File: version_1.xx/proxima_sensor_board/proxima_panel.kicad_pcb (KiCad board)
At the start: 2 copper layers, 83 x 94 mm, 587 parts, among them J1 Conn_01x03, U1 TSOP32156, U2 NE555D

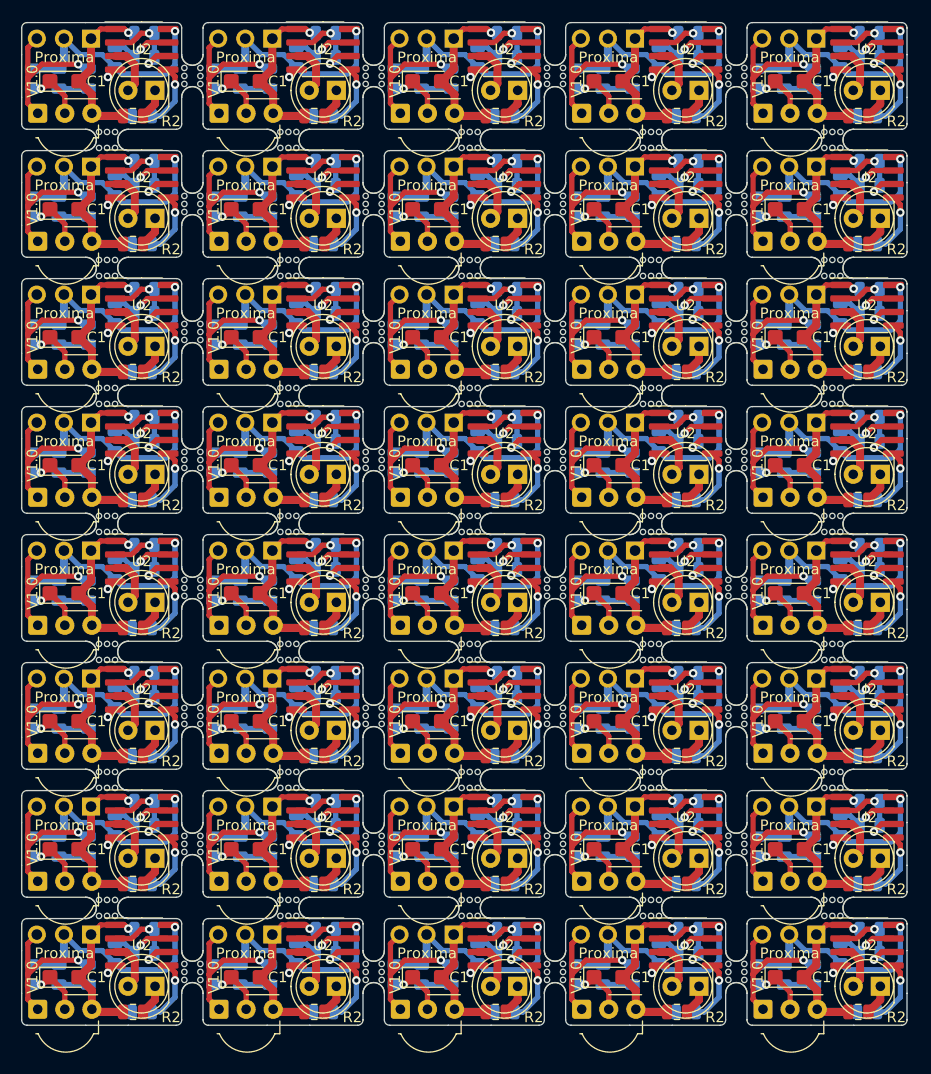
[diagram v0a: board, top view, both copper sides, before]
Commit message: 5mm breakway
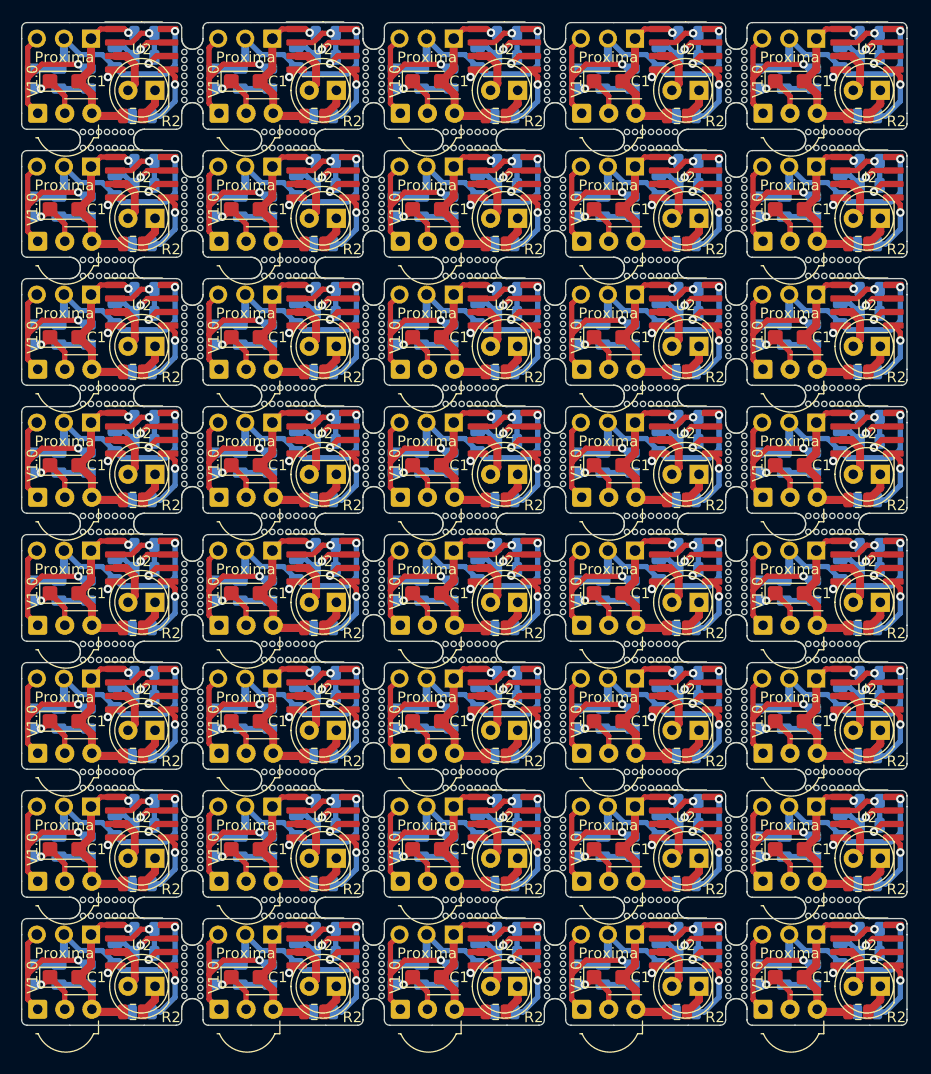
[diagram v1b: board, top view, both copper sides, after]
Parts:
- removed the C3 at (211.5, 134.0)
- removed the C3 at (211.5, 170.0)
- removed the R2 at (176.4, 105.8)
- removed the U1 at (167.5, 117.5)
- removed mouse-bite-2mm-slot (x64): VAL**, Panelization:mouse-bite-2mm-slot
- added ?: , , F.Cu at (165.0, 102.0)
- added ?: , , F.Cu at (199.0, 162.0)
- added ?: , , F.Cu at (182.0, 162.0)
- added ?: , , F.Cu at (165.0, 162.0)
- added ?: , , F.Cu at (148.0, 162.0)
- added ?: , , F.Cu at (199.0, 150.0)
- added ?: , , F.Cu at (182.0, 150.0)
- added ?: , , F.Cu at (165.0, 150.0)
- added ?: , , F.Cu at (148.0, 150.0)
- added ?: , , F.Cu at (199.0, 138.0)
- added ?: , , F.Cu at (182.0, 138.0)
- added ?: , , F.Cu at (199.0, 186.0)
- added ?: , , F.Cu at (165.0, 138.0)
- added ?: , , F.Cu at (148.0, 138.0)
- added ?: , , F.Cu at (199.0, 126.0)
- added ?: , , F.Cu at (182.0, 126.0)
- added ?: , , F.Cu at (165.0, 126.0)
- added ?: , , F.Cu at (148.0, 126.0)
- added ?: , , F.Cu at (199.0, 114.0)
- added ?: , , F.Cu at (182.0, 114.0)
- added ?: , , F.Cu at (165.0, 114.0)
- added ?: , , F.Cu at (148.0, 114.0)
- added ?: , , F.Cu at (182.0, 186.0)
- added ?: , , F.Cu at (199.0, 102.0)
- added ?: , , F.Cu at (182.0, 102.0)
- added ?: , , F.Cu at (208.0, 180.0)
- added ?: , , F.Cu at (191.0, 180.0)
- added ?: , , F.Cu at (174.0, 180.0)
- added ?: , , F.Cu at (157.0, 180.0)
- added ?: , , F.Cu at (140.0, 180.0)
- added ?: , , F.Cu at (208.0, 168.0)
- added ?: , , F.Cu at (191.0, 168.0)
- added ?: , , F.Cu at (174.0, 168.0)
- added ?: , , F.Cu at (165.0, 186.0)
- added ?: , , F.Cu at (157.0, 168.0)
- added ?: , , F.Cu at (140.0, 168.0)
- added ?: , , F.Cu at (208.0, 156.0)
- added ?: , , F.Cu at (191.0, 156.0)
- added ?: , , F.Cu at (174.0, 156.0)
- added ?: , , F.Cu at (157.0, 156.0)
- added ?: , , F.Cu at (140.0, 156.0)
- added ?: , , F.Cu at (208.0, 144.0)
- added ?: , , F.Cu at (191.0, 144.0)
- added ?: , , F.Cu at (174.0, 144.0)
- added ?: , , F.Cu at (148.0, 186.0)
- added ?: , , F.Cu at (157.0, 144.0)
- added ?: , , F.Cu at (140.0, 144.0)
- added ?: , , F.Cu at (208.0, 132.0)
- added ?: , , F.Cu at (191.0, 132.0)
- added ?: , , F.Cu at (174.0, 132.0)
- added ?: , , F.Cu at (157.0, 132.0)
- added ?: , , F.Cu at (140.0, 132.0)
- added ?: , , F.Cu at (208.0, 120.0)
- added ?: , , F.Cu at (191.0, 120.0)
- added ?: , , F.Cu at (174.0, 120.0)
- added ?: , , F.Cu at (199.0, 174.0)
- added ?: , , F.Cu at (157.0, 120.0)
- added ?: , , F.Cu at (140.0, 120.0)
- added ?: , , F.Cu at (208.0, 108.0)
- added ?: , , F.Cu at (191.0, 108.0)
- added ?: , , F.Cu at (174.0, 108.0)
- added ?: , , F.Cu at (157.0, 108.0)
- added ?: , , F.Cu at (140.0, 108.0)
- added ?: , , F.Cu at (148.0, 102.0)
- added ?: , , F.Cu at (182.0, 174.0)
- added ?: , , F.Cu at (165.0, 174.0)
- added ?: , , F.Cu at (148.0, 174.0)
- added R5: 500, Resistor_SMD:R_0805_2012Metric, B.Cu at (138.2, 186.2)
- C3 (x2): renamed from mouse-bite-2mm-slot; value VAL** -> 1.2nF; footprint Panelization:mouse-bite-2mm-slot -> Capacitor_SMD:C_0805_2012Metric; moved to B.Cu
- R2: renamed from mouse-bite-2mm-slot; value VAL** -> 47; footprint Panelization:mouse-bite-2mm-slot -> Resistor_SMD:R_0805_2012Metric
- U1: renamed from R5; value 500 -> TSOP32156; footprint Resistor_SMD:R_0805_2012Metric -> OptoDevice:Vishay_MOLD-3Pin; moved to F.Cu
- moved U1 74.7 mm to (167.5, 117.5), turned to 0 degrees
- moved R2 62.3 mm to (176.4, 105.8), turned to 180 degrees
- moved C3 33.1 mm to (211.5, 134.0), turned to 180 degrees
- moved C3 26.2 mm to (211.5, 170.0), turned to 180 degrees
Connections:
- U1 pad 1: Net-(D2-Pad1) -> OUTPUT_INVERTED
- U1 pad 2: OUTPUT_INVERTED -> Net-(C1-Pad1)
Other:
- outline, holes or cut-outs redrawn

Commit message: panelization 2
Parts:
- removed the ? at (199.0, 162.0)
- removed the ? at (182.0, 162.0)
- removed the ? at (165.0, 162.0)
- removed the ? at (148.0, 162.0)
- removed the ? at (199.0, 150.0)
- removed the ? at (182.0, 150.0)
- removed the ? at (165.0, 150.0)
- removed the ? at (148.0, 150.0)
- removed the ? at (199.0, 138.0)
- removed the ? at (182.0, 138.0)
- removed the ? at (199.0, 186.0)
- removed the ? at (165.0, 138.0)
- removed the ? at (148.0, 138.0)
- removed the ? at (199.0, 126.0)
- removed the ? at (182.0, 126.0)
- removed the ? at (165.0, 126.0)
- removed the ? at (148.0, 126.0)
- removed the ? at (199.0, 114.0)
- removed the ? at (182.0, 186.0)
- removed the ? at (199.0, 102.0)
- removed the ? at (182.0, 102.0)
- removed the ? at (208.0, 180.0)
- removed the ? at (191.0, 180.0)
- removed the ? at (174.0, 180.0)
- removed the ? at (157.0, 180.0)
- removed the ? at (140.0, 180.0)
- removed the ? at (208.0, 168.0)
- removed the ? at (191.0, 168.0)
- removed the ? at (174.0, 168.0)
- removed the ? at (165.0, 186.0)
- removed the ? at (157.0, 168.0)
- removed the ? at (140.0, 168.0)
- removed the ? at (208.0, 156.0)
- removed the ? at (191.0, 156.0)
- removed the ? at (174.0, 156.0)
- removed the ? at (157.0, 156.0)
- removed the ? at (140.0, 156.0)
- removed the ? at (208.0, 144.0)
- removed the ? at (191.0, 144.0)
- removed the ? at (174.0, 144.0)
- removed the ? at (148.0, 186.0)
- removed the ? at (157.0, 144.0)
- removed the ? at (140.0, 144.0)
- removed the ? at (208.0, 132.0)
- removed the ? at (191.0, 132.0)
- removed the ? at (174.0, 132.0)
- removed the ? at (157.0, 132.0)
- removed the ? at (140.0, 132.0)
- removed the ? at (208.0, 120.0)
- removed the ? at (191.0, 120.0)
- removed the ? at (174.0, 120.0)
- removed the ? at (199.0, 174.0)
- removed the ? at (157.0, 120.0)
- removed the ? at (140.0, 120.0)
- removed the ? at (208.0, 108.0)
- removed the ? at (191.0, 108.0)
- removed the ? at (182.0, 174.0)
- removed the ? at (165.0, 174.0)
- removed the ? at (148.0, 174.0)
- removed the C1 at (204.0, 186.5)
- removed the C1 at (136.0, 174.5)
- removed the C1 at (204.0, 162.5)
- removed the C1 at (187.0, 162.5)
- removed the C1 at (170.0, 162.5)
- removed the C1 at (153.0, 162.5)
- removed the C1 at (136.0, 162.5)
- removed the C1 at (204.0, 150.5)
- removed the C1 at (187.0, 150.5)
- removed the C1 at (170.0, 150.5)
- removed the C1 at (153.0, 150.5)
- removed the C1 at (187.0, 186.5)
- removed the C1 at (136.0, 150.5)
- removed the C1 at (204.0, 138.5)
- removed the C1 at (187.0, 138.5)
- removed the C1 at (170.0, 138.5)
- removed the C1 at (153.0, 138.5)
- removed the C1 at (136.0, 138.5)
- removed the C1 at (204.0, 126.5)
- removed the C1 at (187.0, 126.5)
- removed the C1 at (170.0, 126.5)
- removed the C1 at (153.0, 126.5)
- removed the C1 at (170.0, 186.5)
- removed the C1 at (136.0, 126.5)
- removed the C1 at (204.0, 114.5)
- removed the C1 at (187.0, 114.5)
- removed the C1 at (204.0, 102.5)
- removed the C1 at (187.0, 102.5)
- removed the C1 at (153.0, 186.5)
- removed the C1 at (136.0, 186.5)
- removed the C1 at (204.0, 174.5)
- removed the C1 at (187.0, 174.5)
- removed the C1 at (170.0, 174.5)
- removed the C1 at (153.0, 174.5)
- removed the C2 at (211.2, 189.8)
- removed the C2 at (143.2, 177.8)
- removed the C2 at (211.2, 165.8)
- removed the C2 at (194.2, 165.8)
- removed the C2 at (177.2, 165.8)
- removed the C2 at (160.2, 165.8)
- removed the C2 at (143.2, 165.8)
- removed the C2 at (211.2, 153.8)
- removed the C2 at (194.2, 153.8)
- removed the C2 at (177.2, 153.8)
- removed the C2 at (160.2, 153.8)
- removed the C2 at (194.2, 189.8)
- removed the C2 at (143.2, 153.8)
- removed the C2 at (211.2, 141.8)
- removed the C2 at (194.2, 141.8)
- removed the C2 at (177.2, 141.8)
- removed the C2 at (160.2, 141.8)
- removed the C2 at (143.2, 141.8)
- removed the C2 at (211.2, 129.8)
- removed the C2 at (194.2, 129.8)
- removed the C2 at (177.2, 129.8)
- removed the C2 at (160.2, 129.8)
- removed the C2 at (177.2, 189.8)
- removed the C2 at (143.2, 129.8)
- removed the C2 at (211.2, 117.8)
- removed the C2 at (194.2, 117.8)
- removed the C2 at (211.2, 105.8)
- removed the C2 at (194.2, 105.8)
- removed the C2 at (160.2, 189.8)
- removed the C2 at (143.2, 189.8)
- removed the C2 at (211.2, 177.8)
- removed the C2 at (194.2, 177.8)
- removed the C2 at (177.2, 177.8)
- removed the C2 at (160.2, 177.8)
- removed the C3 at (211.5, 182.0)
- removed the C3 at (143.5, 170.0)
- removed the C3 at (211.5, 158.0)
- removed the C3 at (194.5, 158.0)
- removed the C3 at (177.5, 158.0)
- removed the C3 at (160.5, 158.0)
- removed the C3 at (143.5, 158.0)
- removed the C3 at (211.5, 146.0)
- removed the C3 at (194.5, 146.0)
- removed the C3 at (177.5, 146.0)
- removed the C3 at (160.5, 146.0)
- removed the C3 at (194.5, 182.0)
- removed the C3 at (143.5, 146.0)
- removed the C3 at (211.5, 134.0)
- removed the C3 at (194.5, 134.0)
- removed the C3 at (177.5, 134.0)
- removed the C3 at (160.5, 134.0)
- removed the C3 at (143.5, 134.0)
- removed the C3 at (211.5, 122.0)
- removed the C3 at (194.5, 122.0)
- removed the C3 at (177.5, 122.0)
- removed the C3 at (160.5, 122.0)
- removed the C3 at (177.5, 182.0)
- removed the C3 at (143.5, 122.0)
- removed the C3 at (211.5, 110.0)
- removed the C3 at (194.5, 110.0)
- removed the C3 at (211.5, 98.0)
- removed the C3 at (194.5, 98.0)
- removed the C3 at (160.5, 182.0)
- removed the C3 at (143.5, 182.0)
- removed the C3 at (211.5, 170.0)
- removed the C3 at (194.5, 170.0)
- removed the C3 at (177.5, 170.0)
- removed the C3 at (160.5, 170.0)
- removed the D1 at (212.5, 187.3)
- removed the D1 at (144.5, 175.3)
- removed the D1 at (212.5, 163.3)
- removed the D1 at (195.5, 163.3)
- removed the D1 at (178.5, 163.3)
- removed the D1 at (161.5, 163.3)
- removed the D1 at (144.5, 163.3)
- removed the D1 at (212.5, 151.3)
- removed the D1 at (195.5, 151.3)
- removed the D1 at (178.5, 151.3)
- removed the D1 at (161.5, 151.3)
- removed the D1 at (195.5, 187.3)
- removed the D1 at (144.5, 151.3)
- removed the D1 at (212.5, 139.3)
- removed the D1 at (195.5, 139.3)
- removed the D1 at (178.5, 139.3)
- removed the D1 at (161.5, 139.3)
- removed the D1 at (144.5, 139.3)
- removed the D1 at (212.5, 127.3)
- removed the D1 at (195.5, 127.3)
- removed the D1 at (178.5, 127.3)
- removed the D1 at (161.5, 127.3)
- removed the D1 at (178.5, 187.3)
- removed the D1 at (144.5, 127.3)
- removed the D1 at (212.5, 115.3)
- removed the D1 at (195.5, 115.3)
- removed the D1 at (212.5, 103.3)
- removed the D1 at (195.5, 103.3)
- removed the D1 at (161.5, 187.3)
- removed the D1 at (144.5, 187.3)
- removed the D1 at (212.5, 175.3)
- removed the D1 at (195.5, 175.3)
- removed the D1 at (178.5, 175.3)
- removed the D1 at (161.5, 175.3)
- removed the D2 at (203.5, 186.2)
- removed the D2 at (135.5, 174.2)
- removed the D2 at (203.5, 162.2)
- removed the D2 at (186.5, 162.2)
- removed the D2 at (169.5, 162.2)
- removed the D2 at (152.5, 162.2)
- removed the D2 at (135.5, 162.2)
- removed the D2 at (203.5, 150.2)
- removed the D2 at (186.5, 150.2)
- removed the D2 at (169.5, 150.2)
- removed the D2 at (152.5, 150.2)
- removed the D2 at (186.5, 186.2)
- removed the D2 at (135.5, 150.2)
- removed the D2 at (203.5, 138.2)
- removed the D2 at (186.5, 138.2)
- removed the D2 at (169.5, 138.2)
- removed the D2 at (152.5, 138.2)
- removed the D2 at (135.5, 138.2)
- removed the D2 at (203.5, 126.2)
- removed the D2 at (186.5, 126.2)
- removed the D2 at (169.5, 126.2)
- removed the D2 at (152.5, 126.2)
- removed the D2 at (169.5, 186.2)
- removed the D2 at (135.5, 126.2)
- removed the D2 at (203.5, 114.2)
- removed the D2 at (186.5, 114.2)
- removed the D2 at (203.5, 102.2)
- removed the D2 at (186.5, 102.2)
- removed the D2 at (152.5, 186.2)
- removed the D2 at (135.5, 186.2)
- removed the D2 at (203.5, 174.2)
- removed the D2 at (186.5, 174.2)
- removed the D2 at (169.5, 174.2)
- removed the D2 at (152.5, 174.2)
- removed the J1 at (206.5, 182.5)
- removed the J1 at (138.5, 170.5)
- removed the J1 at (206.5, 158.5)
- removed the J1 at (189.5, 158.5)
- removed the J1 at (172.5, 158.5)
- removed the J1 at (155.5, 158.5)
- removed the J1 at (138.5, 158.5)
- removed the J1 at (206.5, 146.5)
- removed the J1 at (189.5, 146.5)
- removed the J1 at (172.5, 146.5)
- removed the J1 at (155.5, 146.5)
- removed the J1 at (189.5, 182.5)
- removed the J1 at (138.5, 146.5)
- removed the J1 at (206.5, 134.5)
- removed the J1 at (189.5, 134.5)
- removed the J1 at (172.5, 134.5)
- removed the J1 at (155.5, 134.5)
- removed the J1 at (138.5, 134.5)
- removed the J1 at (206.5, 122.5)
- removed the J1 at (189.5, 122.5)
- removed the J1 at (172.5, 122.5)
- removed the J1 at (155.5, 122.5)
- removed the J1 at (172.5, 182.5)
- removed the J1 at (138.5, 122.5)
- removed the J1 at (206.5, 110.5)
- removed the J1 at (189.5, 110.5)
- removed the J1 at (206.5, 98.5)
- removed the J1 at (189.5, 98.5)
- removed the J1 at (155.5, 182.5)
- removed the J1 at (138.5, 182.5)
- removed the J1 at (206.5, 170.5)
- removed the J1 at (189.5, 170.5)
- removed the J1 at (172.5, 170.5)
- removed the J1 at (155.5, 170.5)
- removed the R1 at (201.0, 186.2)
- removed the R1 at (133.0, 174.2)
- removed the R1 at (201.0, 162.2)
- removed the R1 at (184.0, 162.2)
- removed the R1 at (167.0, 162.2)
- removed the R1 at (150.0, 162.2)
- removed the R1 at (133.0, 162.2)
- removed the R1 at (201.0, 150.2)
- removed the R1 at (184.0, 150.2)
- removed the R1 at (167.0, 150.2)
- removed the R1 at (150.0, 150.2)
- removed the R1 at (184.0, 186.2)
- removed the R1 at (133.0, 150.2)
- removed the R1 at (201.0, 138.2)
- removed the R1 at (184.0, 138.2)
- removed the R1 at (167.0, 138.2)
- removed the R1 at (150.0, 138.2)
- removed the R1 at (133.0, 138.2)
- removed the R1 at (201.0, 126.2)
- removed the R1 at (184.0, 126.2)
- removed the R1 at (167.0, 126.2)
- removed the R1 at (150.0, 126.2)
- removed the R1 at (167.0, 186.2)
- removed the R1 at (133.0, 126.2)
- removed the R1 at (201.0, 114.2)
- removed the R1 at (184.0, 114.2)
- removed the R1 at (201.0, 102.2)
- removed the R1 at (184.0, 102.2)
- removed the R1 at (150.0, 186.2)
- removed the R1 at (133.0, 186.2)
- removed the R1 at (201.0, 174.2)
- removed the R1 at (184.0, 174.2)
- removed the R1 at (167.0, 174.2)
- removed the R1 at (150.0, 174.2)
- removed the R2 at (210.4, 189.8)
- removed the R2 at (142.4, 177.8)
- removed the R2 at (210.4, 165.8)
- removed the R2 at (193.4, 165.8)
- removed the R2 at (176.4, 165.8)
- removed the R2 at (159.4, 165.8)
- removed the R2 at (142.4, 165.8)
- removed the R2 at (210.4, 153.8)
- removed the R2 at (193.4, 153.8)
- removed the R2 at (176.4, 153.8)
- removed the R2 at (159.4, 153.8)
- removed the R2 at (193.4, 189.8)
- removed the R2 at (142.4, 153.8)
- removed the R2 at (210.4, 141.8)
- removed the R2 at (193.4, 141.8)
- removed the R2 at (176.4, 141.8)
- removed the R2 at (159.4, 141.8)
- removed the R2 at (142.4, 141.8)
- removed the R2 at (210.4, 129.8)
- removed the R2 at (193.4, 129.8)
- removed the R2 at (176.4, 129.8)
- removed the R2 at (159.4, 129.8)
- removed the R2 at (176.4, 189.8)
- removed the R2 at (142.4, 129.8)
- removed the R2 at (210.4, 117.8)
- removed the R2 at (193.4, 117.8)
- removed the R2 at (210.4, 105.8)
- removed the R2 at (193.4, 105.8)
- removed the R2 at (159.4, 189.8)
- removed the R2 at (142.4, 189.8)
- removed the R2 at (210.4, 177.8)
- removed the R2 at (193.4, 177.8)
- removed the R2 at (176.4, 177.8)
- removed the R2 at (159.4, 177.8)
- removed the R3 at (208.8, 184.2)
- removed the R3 at (140.8, 172.2)
- removed the R3 at (208.8, 160.2)
- removed the R3 at (191.8, 160.2)
- removed the R3 at (174.8, 160.2)
- removed the R3 at (157.8, 160.2)
- removed the R3 at (140.8, 160.2)
- removed the R3 at (208.8, 148.2)
- removed the R3 at (191.8, 148.2)
- removed the R3 at (174.8, 148.2)
- removed the R3 at (157.8, 148.2)
- removed the R3 at (191.8, 184.2)
- removed the R3 at (140.8, 148.2)
- removed the R3 at (208.8, 136.2)
- removed the R3 at (191.8, 136.2)
- removed the R3 at (174.8, 136.2)
- removed the R3 at (157.8, 136.2)
- removed the R3 at (140.8, 136.2)
- removed the R3 at (208.8, 124.2)
- removed the R3 at (191.8, 124.2)
- removed the R3 at (174.8, 124.2)
- removed the R3 at (157.8, 124.2)
- removed the R3 at (174.8, 184.2)
- removed the R3 at (140.8, 124.2)
- removed the R3 at (208.8, 112.2)
- removed the R3 at (191.8, 112.2)
- removed the R3 at (208.8, 100.2)
- removed the R3 at (191.8, 100.2)
- removed the R3 at (157.8, 184.2)
- removed the R3 at (140.8, 184.2)
- removed the R3 at (208.8, 172.2)
- removed the R3 at (191.8, 172.2)
- removed the R3 at (174.8, 172.2)
- removed the R3 at (157.8, 172.2)
- removed the R4 at (211.5, 184.2)
- removed the R4 at (143.5, 172.2)
- removed the R4 at (211.5, 160.2)
- removed the R4 at (194.5, 160.2)
- removed the R4 at (177.5, 160.2)
- removed the R4 at (160.5, 160.2)
- removed the R4 at (143.5, 160.2)
- removed the R4 at (211.5, 148.2)
- removed the R4 at (194.5, 148.2)
- removed the R4 at (177.5, 148.2)
- removed the R4 at (160.5, 148.2)
- removed the R4 at (194.5, 184.2)
- removed the R4 at (143.5, 148.2)
- removed the R4 at (211.5, 136.2)
- removed the R4 at (194.5, 136.2)
- removed the R4 at (177.5, 136.2)
- removed the R4 at (160.5, 136.2)
- removed the R4 at (143.5, 136.2)
- removed the R4 at (211.5, 124.2)
- removed the R4 at (194.5, 124.2)
- removed the R4 at (177.5, 124.2)
- removed the R4 at (160.5, 124.2)
- removed the R4 at (177.5, 184.2)
- removed the R4 at (143.5, 124.2)
- removed the R4 at (211.5, 112.2)
- removed the R4 at (194.5, 112.2)
- removed the R4 at (211.5, 100.2)
- removed the R4 at (194.5, 100.2)
- removed the R4 at (160.5, 184.2)
- removed the R4 at (143.5, 184.2)
- removed the R4 at (211.5, 172.2)
- removed the R4 at (194.5, 172.2)
- removed the R4 at (177.5, 172.2)
- removed the R4 at (160.5, 172.2)
- removed the R5 at (206.2, 186.2)
- removed the R5 at (138.2, 174.2)
- removed the R5 at (206.2, 162.2)
- removed the R5 at (189.2, 162.2)
- removed the R5 at (172.2, 162.2)
- removed the R5 at (155.2, 162.2)
- removed the R5 at (138.2, 162.2)
- removed the R5 at (206.2, 150.2)
- removed the R5 at (189.2, 150.2)
- removed the R5 at (172.2, 150.2)
- removed the R5 at (155.2, 150.2)
- removed the R5 at (189.2, 186.2)
- removed the R5 at (138.2, 150.2)
- removed the R5 at (206.2, 138.2)
- removed the R5 at (189.2, 138.2)
- removed the R5 at (172.2, 138.2)
- removed the R5 at (155.2, 138.2)
- removed the R5 at (138.2, 138.2)
- removed the R5 at (206.2, 126.2)
- removed the R5 at (189.2, 126.2)
- removed the R5 at (172.2, 126.2)
- removed the R5 at (155.2, 126.2)
- removed the R5 at (172.2, 186.2)
- removed the R5 at (138.2, 126.2)
- removed the R5 at (206.2, 114.2)
- removed the R5 at (189.2, 114.2)
- removed the R5 at (206.2, 102.2)
- removed the R5 at (189.2, 102.2)
- removed the R5 at (155.2, 186.2)
- removed the R5 at (138.2, 186.2)
- removed the R5 at (206.2, 174.2)
- removed the R5 at (189.2, 174.2)
- removed the R5 at (172.2, 174.2)
- removed the R5 at (155.2, 174.2)
- removed the U1 at (201.5, 189.5)
- removed the U1 at (133.5, 177.5)
- removed the U1 at (201.5, 165.5)
- removed the U1 at (184.5, 165.5)
- removed the U1 at (167.5, 165.5)
- removed the U1 at (150.5, 165.5)
- removed the U1 at (133.5, 165.5)
- removed the U1 at (201.5, 153.5)
- removed the U1 at (184.5, 153.5)
- removed the U1 at (167.5, 153.5)
- removed the U1 at (150.5, 153.5)
- removed the U1 at (184.5, 189.5)
- removed the U1 at (133.5, 153.5)
- removed the U1 at (201.5, 141.5)
- removed the U1 at (184.5, 141.5)
- removed the U1 at (167.5, 141.5)
- removed the U1 at (150.5, 141.5)
- removed the U1 at (133.5, 141.5)
- removed the U1 at (201.5, 129.5)
- removed the U1 at (184.5, 129.5)
- removed the U1 at (167.5, 129.5)
- removed the U1 at (150.5, 129.5)
- removed the U1 at (167.5, 189.5)
- removed the U1 at (133.5, 129.5)
- removed the U1 at (201.5, 117.5)
- removed the U1 at (184.5, 117.5)
- removed the U1 at (201.5, 105.5)
- removed the U1 at (184.5, 105.5)
- removed the U1 at (150.5, 189.5)
- removed the U1 at (133.5, 189.5)
- removed the U1 at (201.5, 177.5)
- removed the U1 at (184.5, 177.5)
- removed the U1 at (167.5, 177.5)
- removed the U1 at (150.5, 177.5)
- removed the U2 at (211.2, 183.5)
- removed the U2 at (143.2, 171.5)
- removed the U2 at (211.2, 159.5)
- removed the U2 at (194.2, 159.5)
- removed the U2 at (177.2, 159.5)
- removed the U2 at (160.2, 159.5)
- removed the U2 at (143.2, 159.5)
- removed the U2 at (211.2, 147.5)
- removed the U2 at (194.2, 147.5)
- removed the U2 at (177.2, 147.5)
- removed the U2 at (160.2, 147.5)
- removed the U2 at (194.2, 183.5)
- removed the U2 at (143.2, 147.5)
- removed the U2 at (211.2, 135.5)
- removed the U2 at (194.2, 135.5)
- removed the U2 at (177.2, 135.5)
- removed the U2 at (160.2, 135.5)
- removed the U2 at (143.2, 135.5)
- removed the U2 at (211.2, 123.5)
- removed the U2 at (194.2, 123.5)
- removed the U2 at (177.2, 123.5)
- removed the U2 at (160.2, 123.5)
- removed the U2 at (177.2, 183.5)
- removed the U2 at (143.2, 123.5)
- removed the U2 at (211.2, 111.5)
- removed the U2 at (194.2, 111.5)
- removed the U2 at (211.2, 99.5)
- removed the U2 at (194.2, 99.5)
- removed the U2 at (160.2, 183.5)
- removed the U2 at (143.2, 183.5)
- removed the U2 at (211.2, 171.5)
- removed the U2 at (194.2, 171.5)
- removed the U2 at (177.2, 171.5)
- removed the U2 at (160.2, 171.5)
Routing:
- net VCC: track 948.4 -> 142.3 mm, vias 80 -> 12
- net GND: track 778.0 -> 116.7 mm, vias 40 -> 6
- net OUTPUT_INVERTED: track 565.6 -> 84.8 mm, vias 40 -> 6
- net Net-(C3-Pad1): track 397.0 -> 59.5 mm, vias 80 -> 12
- net Net-(R3-Pad2): track 241.3 -> 36.2 mm, vias 40 -> 6
- net Net-(C2-Pad1): track 239.9 -> 36.0 mm, vias 40 -> 6
- net Net-(C1-Pad1): track 220.8 -> 33.1 mm, vias 40 -> 6
- net SQUARE_WAVE_SIGNAL: track 193.1 -> 29.0 mm
- net Net-(D1-Pad1): track 114.6 -> 17.2 mm
- net Net-(D2-Pad1): track 110.0 -> 16.5 mm
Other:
- board size 83 x 94 mm -> 53.5 x 22 mm
- board text added: "JLCJLCJLCJLC"
